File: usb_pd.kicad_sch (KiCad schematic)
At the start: 81 parts, among them Q1 Q_NMOS_DGS, Q2 Q_NMOS_DGS, Q3 Q_NMOS_DGS, Q4 Q_NMOS_DGS, U5 TPS5403DR, U6 MP28167GQ-P, U7 BQ25731

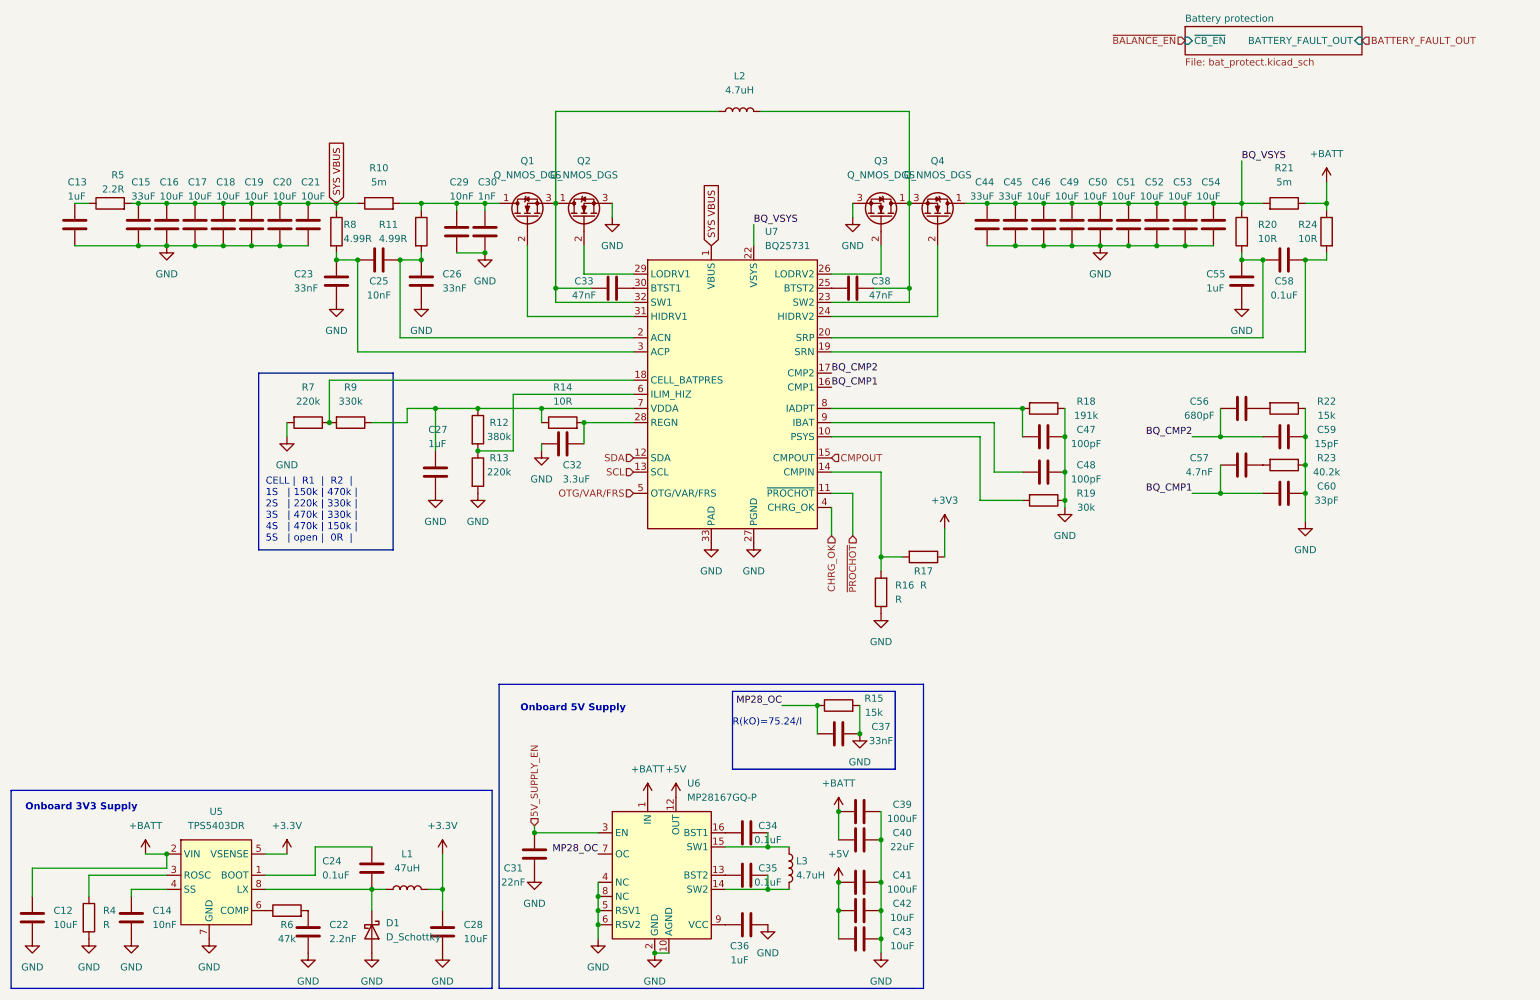
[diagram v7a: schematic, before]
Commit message: PI LC lowpass filter, added CP2012 reset, added connectors
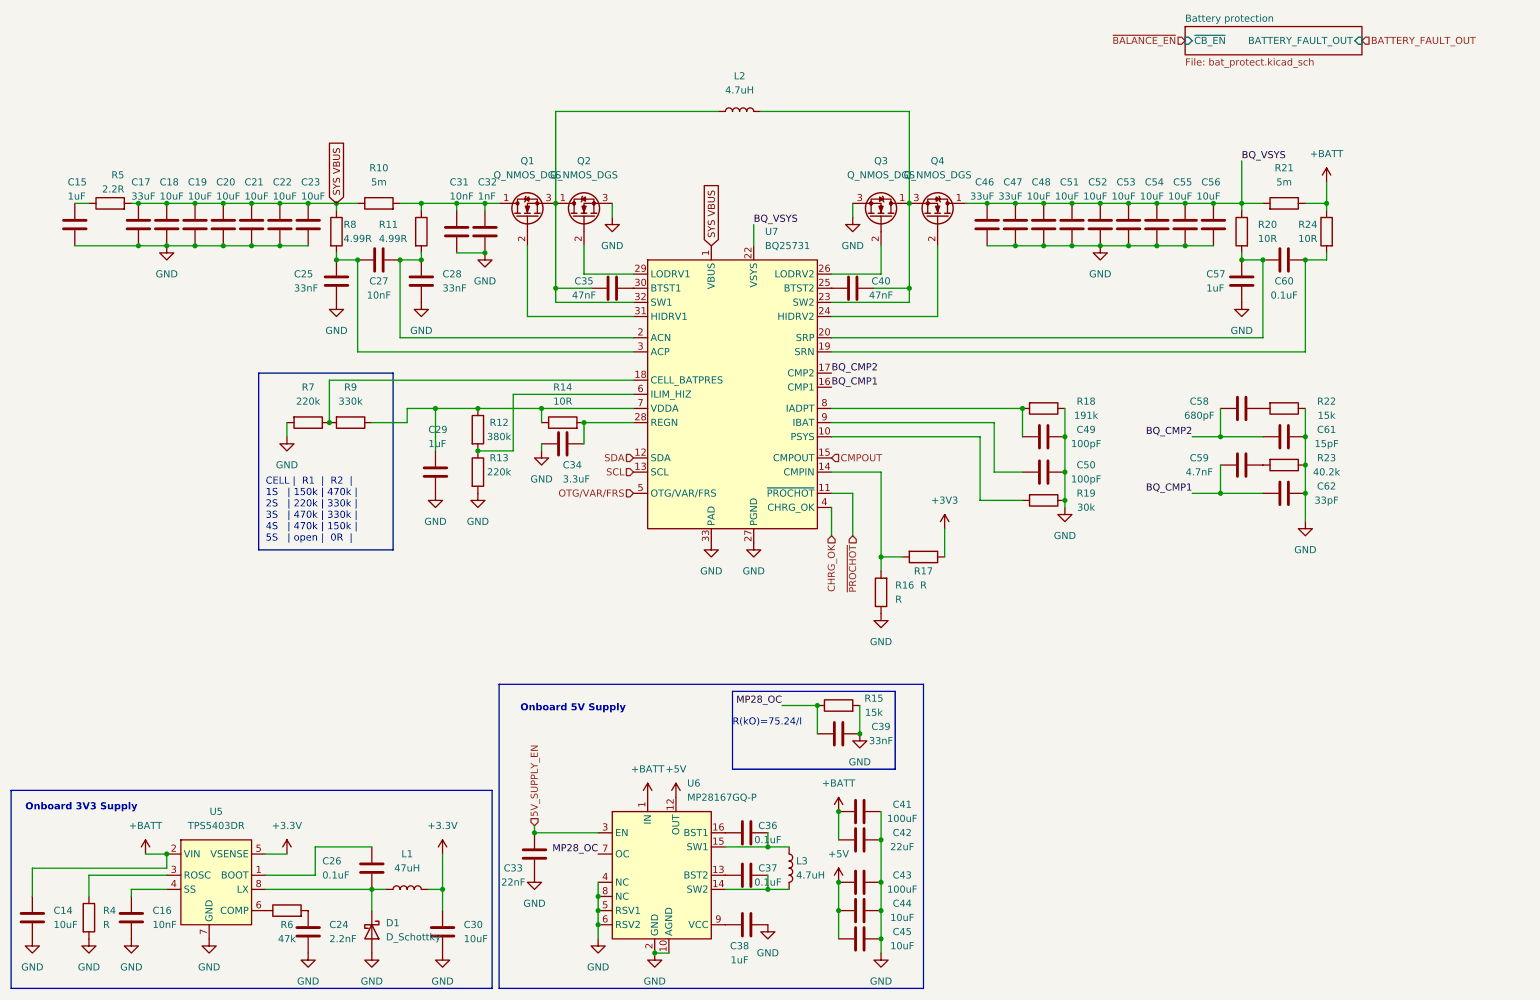
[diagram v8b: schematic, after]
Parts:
- renumbered C12 to C14, C13 to C15, C14 to C16, C15 to C17, C16 to C18, C17 to C19, C18 to C20, C19 to C21, C20 to C22, C21 to C23, C22 to C24, C23 to C25, C24 to C26, C25 to C27, C26 to C28, C27 to C29, C28 to C30, C29 to C31, C30 to C32, C31 to C33, C32 to C34, C33 to C35, C34 to C36, C35 to C37, C36 to C38, C37 to C39, C38 to C40, C39 to C41, C40 to C42, C41 to C43, C42 to C44, C43 to C45, C44 to C46, C45 to C47, C46 to C48, C47 to C49, C48 to C50, C49 to C51, C50 to C52, C51 to C53, C52 to C54, C53 to C55, C54 to C56, C55 to C57, C56 to C58, C57 to C59, C58 to C60, C59 to C61, C60 to C62
